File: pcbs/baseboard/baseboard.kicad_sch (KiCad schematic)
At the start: 22 parts, among them J1 Power, J3 gpio_breakout, J4 SWD, J5 DC, SW1 SW_Push, U1 Pico

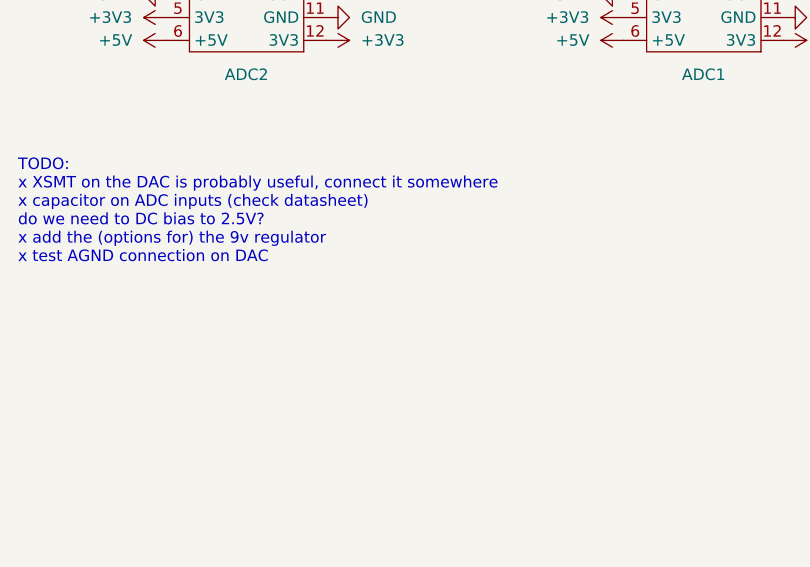
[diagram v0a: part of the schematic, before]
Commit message: Expand baseboard + devkit
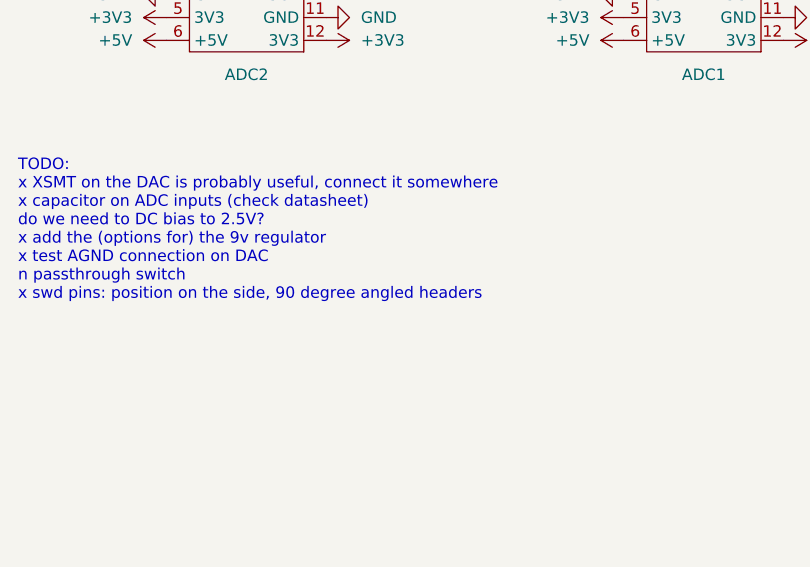
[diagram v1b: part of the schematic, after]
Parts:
- JACK1, JACK2, JACK3: footprint rytmos:Jack_6.3mm -> rytmos:SlimJack6.3
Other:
- note added: "TODO: x XSMT on the DAC is probably useful, connect it somewhere x capacitor on ADC inputs (check datasheet) do we need to DC bias to 2.5V? x add the (options for) the 9v regulator x test AGND connection on DAC n passthrough switch x swd pins: position on the side, 90 degree angled headers"
- note removed: "TODO: x XSMT on the DAC is probably useful, connect it somewhere x capacitor on ADC inputs (check datasheet) do we need to DC bias to 2.5V? x add the (options for) the 9v regulator x test AGND connection on DAC"
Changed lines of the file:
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@@
 	(generator_version "9.0")
 	(paper "A4")
-	(text "TODO:\nx XSMT on the DAC is probably useful, connect it somewhere\nx capacitor on ADC inputs (check datasheet)\ndo we need to DC bias to 2.5V?\nx add the (options for) the 9v regulator\nx test AGND connection on DAC"
+	(text "TODO:\nx XSMT on the DAC is probably useful, connect it somewhere\nx capacitor on ADC inputs (check datasheet)\ndo we need to DC bias to 2.5V?\nx add the (options for) the 9v regulator\nx test AGND connection on DAC\nn passthrough switch\nx swd pins: position on the side, 90 degree angled headers"
 		(exclude_from_sim no)
 		(at 19.05 81.788 0)
@@
 			)
 		)
-		(property "Footprint" "rytmos:Jack_6.3mm"
+		(property "Footprint" "rytmos:SlimJack6.3"
 			(at 43.18 26.67 90)
 			(effects
@@
 			)
 		)
-		(property "Footprint" "rytmos:Jack_6.3mm"
+		(property "Footprint" "rytmos:SlimJack6.3"
 			(at 93.98 26.67 90)
 			(effects
@@
 			)
 		)
-		(property "Footprint" "rytmos:Jack_6.3mm"
+		(property "Footprint" "rytmos:SlimJack6.3"
 			(at 205.74 52.07 90)
 			(effects

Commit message: Order baseboard and devkit
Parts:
- added JP1, JP3, JP4, JP5: ~, Jumper:SolderJumper-2_P1.3mm_Open_RoundedPad1.0x1.5mm, symbol Jumper:SolderJumper_2_Open
- added JP2, JP6: ~, Jumper:SolderJumper-2_P1.3mm_Bridged_RoundedPad1.0x1.5mm, symbol Jumper:SolderJumper_2_Bridged
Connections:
- net +9V: now also JP1.2 (B), JP3.2 (B), JP6.2 (B); no longer J5.1
- net GND: now also JP2.2 (B), JP4.2 (B), JP5.2 (B); no longer J5.3
- net at J5.2: now also JP5.1 (A), JP6.1 (A)
- new net: J5.3, JP3.1 (A), JP4.1 (A)
- new net: J5.1, JP1.1 (A), JP2.1 (A)
- no-connect marks 25 -> 24
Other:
- note added: "TODO: x XSMT on the DAC is probably useful, connect it somewhere x capacitor on ADC inputs (check datasheet) x do we need to DC bias to 2.5V? x add the (options for) the 9v regulator x test AGND connection on DAC n passthrough switch x swd pins: position on the side, 90 degree angled headers x fix ADC footprint, analog inputs are incorrect x double check DC barrel jack footprint"
- note removed: "TODO: x XSMT on the DAC is probably useful, connect it somewhere x capacitor on ADC inputs (check datasheet) do we need to DC bias to 2.5V? x add the (options for) the 9v regulator x test AGND connection on DAC n passthrough switch x swd pins: position on the side, 90 degree angled headers"
- moved on the sheet: J5
